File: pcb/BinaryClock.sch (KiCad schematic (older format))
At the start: 18 parts, among them CON1 AVR-ISP-6, CON2 BARREL_JACK, IC1 ATMEGA328P-A, U1 MC33269, U2 DS3231, U3 clock_header, U4 clock_header, U5 clock_header, Y1 16MHz

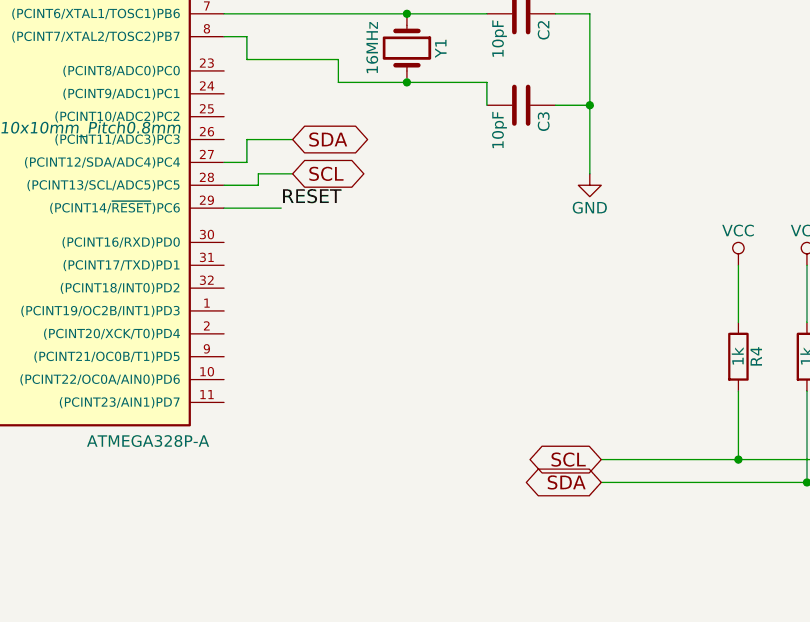
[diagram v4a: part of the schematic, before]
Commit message: Added schematic connections for an external led on/off switch
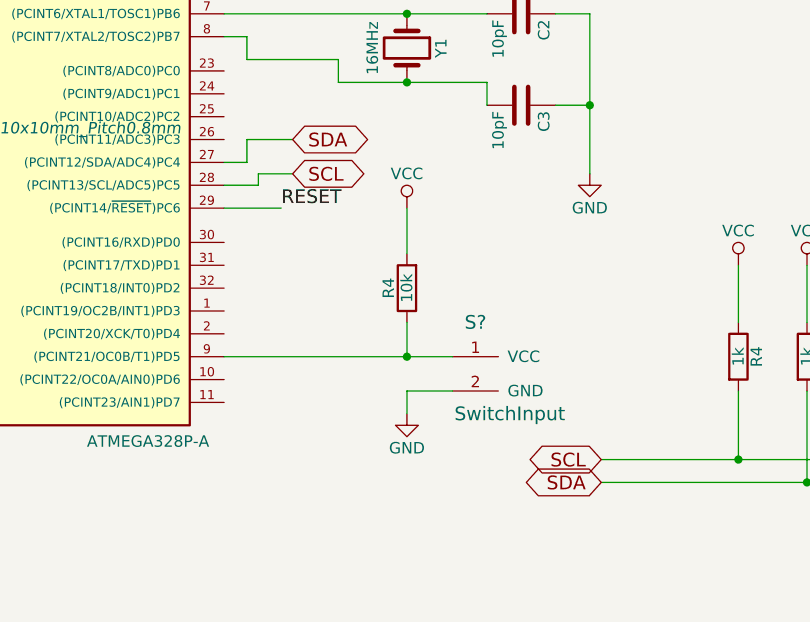
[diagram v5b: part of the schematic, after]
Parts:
- added R4: 10k, symbol R
- added S?: SwitchInput, symbol SwitchInput
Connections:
- net GND: now also S?.2 (GND)
- net VCC: now also R4.2
- net at IC1.9 ((PCINT21/OC0B/T1)PD5): now also R4.1, S?.1 (VCC)
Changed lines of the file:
@@
 	1    0    0    -1
 $EndComp
-Wire Wire Line
-	7950 4800 8950 4800
-Wire Wire Line
-	7950 4900 8950 4900
-Connection ~ 8550 4800
-Connection ~ 8850 4900
-Wire Wire Line
-	9450 5400 9450 5550
-Wire Wire Line
-	9950 5100 10250 5100
-Wire Wire Line
-	10250 5400 10250 5550
-Wire Wire Line
-	7950 2150 8350 2150
-Wire Wire Line
-	8350 2350 7950 2350
-Wire Wire Line
-	7950 2550 8350 2550
-Wire Wire Line
-	6300 2850 7450 2850
-Connection ~ 7100 2850
-Wire Wire Line
-	7750 2850 7900 2850
-Wire Wire Line
-	7900 2850 7900 3550
-Wire Wire Line
-	6400 3050 6800 3050
-Wire Wire Line
-	6800 3050 6800 3150
-Wire Wire Line
-	6800 3150 7450 3150
-Wire Wire Line
-	7450 3150 7450 3250
-Connection ~ 7100 3150
-Wire Wire Line
-	7750 3250 7900 3250
-Connection ~ 7900 3250
-Wire Wire Line
-	7650 2150 6600 2150
-Wire Wire Line
-	6600 2150 6600 2250
-Wire Wire Line
-	6600 2250 6300 2250
-Wire Wire Line
-	7650 2350 6300 2350
-Wire Wire Line
-	7650 2550 6600 2550
-Wire Wire Line
-	6600 2550 6600 2450
-Wire Wire Line
-	6600 2450 6300 2450
-Wire Wire Line
-	8550 4500 8550 4800
-Wire Wire Line
-	8850 3950 8850 4200
-Wire Wire Line
-	8850 4500 8850 4900
-Wire Wire Line
-	4050 1900 4050 2550
-Wire Wire Line
-	4050 2350 4400 2350
-Wire Wire Line
-	4400 2250 4050 2250
-Connection ~ 4050 2250
-Wire Wire Line
-	4400 4350 4100 4350
-Wire Wire Line
-	4400 4450 4100 4450
-Connection ~ 4100 4450
-Wire Wire Line
-	4100 4550 4400 4550
-Connection ~ 4100 4550
-Connection ~ 4100 4350
-Wire Wire Line
-	6400 3050 6400 2950
-Wire Wire Line
-	6400 2950 6300 2950
 $Comp
 L ATMEGA328P-A IC1
@@
 Text Label 6350 2650 0    60   ~ 0
 MISO
-Wire Wire Line
-	6350 2650 6300 2650
-Wire Wire Line
-	6300 2550 6350 2550
 Text Label 6350 2750 0    60   ~ 0
 SCK
@@
 Text Label 6550 3700 0    60   ~ 0
 RESET
-Wire Wire Line
-	6300 2750 6350 2750
-Wire Wire Line
-	6300 3500 6400 3500
-Wire Wire Line
-	6400 3500 6400 3400
-Wire Wire Line
-	6400 3400 6600 3400
-Wire Wire Line
-	6300 3600 6450 3600
-Wire Wire Line
-	6450 3600 6450 3550
-Wire Wire Line
-	6450 3550 6600 3550
 Text Label 2800 3250 0    60   ~ 0
 MOSI
 Text Label 1000 3350 2    60   ~ 0
 RESET
-Wire Wire Line
-	1750 3150 2150 3150
-Wire Wire Line
-	2150 3250 1750 3250
-Wire Wire Line
-	1000 3350 2150 3350
-Wire Wire Line
-	2400 3250 2800 3250
 $Comp
 L VCC #PWR09
@@
 	1    0    0    -1
 $EndComp
-Wire Wire Line
-	2750 2650 2750 3150
-Wire Wire Line
-	2750 3150 2400 3150
 $Comp
 L GND #PWR010
@@
 	1    0    0    -1
 $EndComp
-Wire Wire Line
-	2750 3600 2750 3350
-Wire Wire Line
-	2750 3350 2400 3350
 $Comp
 L clock_header U3
@@
 Text Label 9800 2750 2    60   ~ 0
 LED3
-Wire Wire Line
-	9950 1450 9800 1450
-Wire Wire Line
-	9950 2100 9800 2100
-Wire Wire Line
-	10000 2750 9800 2750
 $Comp
 L GND #PWR011
@@
 	1    0    0    -1
 $EndComp
-Wire Wire Line
-	9250 1250 9250 2850
-Wire Wire Line
-	9250 2850 10000 2850
-Wire Wire Line
-	9950 2200 9250 2200
-Connection ~ 9250 2200
-Wire Wire Line
-	9950 1550 9250 1550
-Connection ~ 9250 1550
-Wire Wire Line
-	9400 1650 9400 3100
-Wire Wire Line
-	9400 1650 9950 1650
-Wire Wire Line
-	9950 2300 9400 2300
-Connection ~ 9400 2300
-Wire Wire Line
-	10000 2950 9400 2950
-Connection ~ 9400 2950
 Text GLabel 7950 4800 0    60   BiDi ~ 0
 SCL
@@
 	1    0    0    -1
 $EndComp
-Wire Wire Line
-	2700 1800 2700 2150
 $Comp
 L VCC #PWR013
@@
 Text Label 1900 1500 2    60   ~ 0
 VIN
-Wire Wire Line
-	1900 1500 2300 1500
-Wire Wire Line
-	3100 1500 3500 1500
-Wire Wire Line
-	4100 4350 4100 4800
 $Comp
 L MC33269 U1
@@
 	1    0    0    -1
 $EndComp
-Wire Wire Line
-	2700 2150 3100 2150
-Wire Wire Line
-	3100 2150 3100 2050
-Wire Wire Line
-	3500 1500 3500 1900
-Connection ~ 3350 1500
-Wire Wire Line
-	6550 3700 6300 3700
-Wire Wire Line
-	2750 2750 1300 2750
-Wire Wire Line
-	1300 2750 1300 2800
-Connection ~ 2750 2750
 $Comp
 L R R6
@@
 	1    0    0    -1
 $EndComp
-Wire Wire Line
-	1300 3100 1300 3350
-Connection ~ 1300 3350
-Wire Wire Line
-	4050 2550 4400 2550
-Connection ~ 4050 2350
-Wire Wire Line
-	8550 3950 8550 4200
 $Comp
 L BARREL_JACK CON2
@@
 	1    0    0    -1
 $EndComp
-Wire Wire Line
-	1350 1100 1550 1100
-Wire Wire Line
-	1550 1100 1550 1200
-Wire Wire Line
-	1350 900  1550 900
-Wire Wire Line
-	1550 900  1550 700
 Text Label 1550 700  2    60   ~ 0
 VIN
 Text Label 9250 1250 2    60   ~ 0
 VIN
+$Comp
+L R R4
+U 1 1 5929A12D
+P 7100 4050
+F 0 "R4" V 7180 4050 50  0000 C CNN
+F 1 "10k" V 7100 4050 50  0000 C CNN
+F 2 "" V 7030 4050 50  0000 C CNN
+F 3 "" H 7100 4050 50  0000 C CNN
+	1    7100 4050
+	-1   0    0    1
+$EndComp
+Wire Wire Line
+	7950 4800 8950 4800
+Wire Wire Line
+	7950 4900 8950 4900
+Connection ~ 8550 4800
+Connection ~ 8850 4900
+Wire Wire Line
+	9450 5400 9450 5550
+Wire Wire Line
+	9950 5100 10250 5100
+Wire Wire Line
+	10250 5400 10250 5550
+Wire Wire Line
+	7950 2150 8350 2150
+Wire Wire Line
+	8350 2350 7950 2350
+Wire Wire Line
+	7950 2550 8350 2550
+Wire Wire Line
+	6300 2850 7450 2850
+Connection ~ 7100 2850
+Wire Wire Line
+	7750 2850 7900 2850
+Wire Wire Line
+	7900 2850 7900 3550
+Wire Wire Line
+	6400 3050 6800 3050
+Wire Wire Line
+	6800 3050 6800 3150
+Wire Wire Line
+	6800 3150 7450 3150
+Wire Wire Line
+	7450 3150 7450 3250
+Connection ~ 7100 3150
+Wire Wire Line
+	7750 3250 7900 3250
+Connection ~ 7900 3250
+Wire Wire Line
+	7650 2150 6600 2150
+Wire Wire Line
+	6600 2150 6600 2250
+Wire Wire Line
+	6600 2250 6300 2250
+Wire Wire Line
+	7650 2350 6300 2350
+Wire Wire Line
+	7650 2550 6600 2550
+Wire Wire Line
+	6600 2550 6600 2450
+Wire Wire Line
+	6600 2450 6300 2450
+Wire Wire Line
+	8550 4500 8550 4800
+Wire Wire Line
+	8850 3950 8850 4200
+Wire Wire Line
+	8850 4500 8850 4900
+Wire Wire Line
+	4050 1900 4050 2550
+Wire Wire Line
+	4050 2350 4400 2350
+Wire Wire Line
+	4400 2250 4050 2250
+Connection ~ 4050 2250
+Wire Wire Line
+	4400 4350 4100 4350
+Wire Wire Line
+	4400 4450 4100 4450
+Connection ~ 4100 4450
+Wire Wire Line
+	4100 4550 4400 4550
+Connection ~ 4100 4550
+Connection ~ 4100 4350
+Wire Wire Line
+	6400 3050 6400 2950
+Wire Wire Line
+	6400 2950 6300 2950
+Wire Wire Line
+	6350 2650 6300 2650
+Wire Wire Line
+	6300 2550 6350 2550
+Wire Wire Line
+	6300 2750 6350 2750
+Wire Wire Line
+	6300 3500 6400 3500
+Wire Wire Line
+	6400 3500 6400 3400
+Wire Wire Line
+	6400 3400 6600 3400
+Wire Wire Line
+	6300 3600 6450 3600
+Wire Wire Line
+	6450 3600 6450 3550
+Wire Wire Line
+	6450 3550 6600 3550
+Wire Wire Line
+	1750 3150 2150 3150
+Wire Wire Line
+	2150 3250 1750 3250
+Wire Wire Line
+	1000 3350 2150 3350
+Wire Wire Line
+	2400 3250 2800 3250
+Wire Wire Line
+	2750 2650 2750 3150
+Wire Wire Line
+	2750 3150 2400 3150
+Wire Wire Line
+	2750 3600 2750 3350
+Wire Wire Line
+	2750 3350 2400 3350
+Wire Wire Line
+	9950 1450 9800 1450
+Wire Wire Line
+	9950 2100 9800 2100
+Wire Wire Line
+	10000 2750 9800 2750
+Wire Wire Line
+	9250 1250 9250 2850
+Wire Wire Line
+	9250 2850 10000 2850
+Wire Wire Line
+	9950 2200 9250 2200
+Connection ~ 9250 2200
+Wire Wire Line
+	9950 1550 9250 1550
+Connection ~ 9250 1550
+Wire Wire Line
+	9400 1650 9400 3100
+Wire Wire Line
+	9400 1650 9950 1650
+Wire Wire Line
+	9950 2300 9400 2300
+Connection ~ 9400 2300
+Wire Wire Line
+	10000 2950 9400 2950
+Connection ~ 9400 2950
+Wire Wire Line
+	2700 1800 2700 2150
+Wire Wire Line
+	1900 1500 2300 1500
+Wire Wire Line
+	3100 1500 3500 1500
+Wire Wire Line
+	4100 4350 4100 4800
+Wire Wire Line
+	2700 2150 3100 2150
+Wire Wire Line
+	3100 2150 3100 2050
+Wire Wire Line
+	3500 1500 3500 1900
+Connection ~ 3350 1500
+Wire Wire Line
+	6550 3700 6300 3700
+Wire Wire Line
+	2750 2750 1300 2750
+Wire Wire Line
+	1300 2750 1300 2800
+Connection ~ 2750 2750
+Wire Wire Line
+	1300 3100 1300 3350
+Connection ~ 1300 3350
+Wire Wire Line
+	4050 2550 4400 2550
+Connection ~ 4050 2350
+Wire Wire Line
+	8550 3950 8550 4200
+Wire Wire Line
+	1350 1100 1550 1100
+Wire Wire Line
+	1550 1100 1550 1200
+Wire Wire Line
+	1350 900  1550 900
+Wire Wire Line
+	1550 900  1550 700
+$Comp
+L GND #PWR?
+U 1 1 5929BBA2
+P 7100 4600
+F 0 "#PWR?" H 7100 4350 50  0001 C CNN
+F 1 "GND" H 7100 4450 50  0000 C CNN
+F 2 "" H 7100 4600 50  0000 C CNN
+F 3 "" H 7100 4600 50  0000 C CNN
+	1    7100 4600
+	1    0    0    -1
+$EndComp
+$Comp
+L VCC #PWR?
+U 1 1 5929BE36
+P 7100 3700
+F 0 "#PWR?" H 7100 3550 50  0001 C CNN
+F 1 "VCC" H 7100 3850 50  0000 C CNN
+F 2 "" H 7100 3700 50  0000 C CNN
+F 3 "" H 7100 3700 50  0000 C CNN
+	1    7100 3700
+	1    0    0    -1
+$EndComp
+Wire Wire Line
+	7100 3700 7100 3900
+$Comp
+L SwitchInput S?
+U 1 1 5929C320
+P 7300 4350
+F 0 "S?" H 7400 4500 60  0000 C CNN
+F 1 "SwitchInput" H 7550 4100 60  0000 C CNN
+F 2 "" H 7300 4350 60  0001 C CNN
+F 3 "" H 7300 4350 60  0001 C CNN
+	1    7300 4350
+	1    0    0    -1
+$EndComp
+Wire Wire Line
+	6300 4350 7300 4350
+Wire Wire Line
+	7100 4200 7100 4350
+Connection ~ 7100 4350
+Wire Wire Line
+	7300 4500 7100 4500
+Wire Wire Line
+	7100 4500 7100 4600
 $EndSCHEMATC
